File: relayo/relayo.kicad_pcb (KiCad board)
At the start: 2 copper layers, 34 parts, among them J1 24V, J2 Conn_01x02, J3 Conn_01x02, J4 Conn_01x02, J5 DB9_Female, Q1 TIP122, Q2 TIP122, Q3 TIP122, Q4 TIP122, U1 Buck

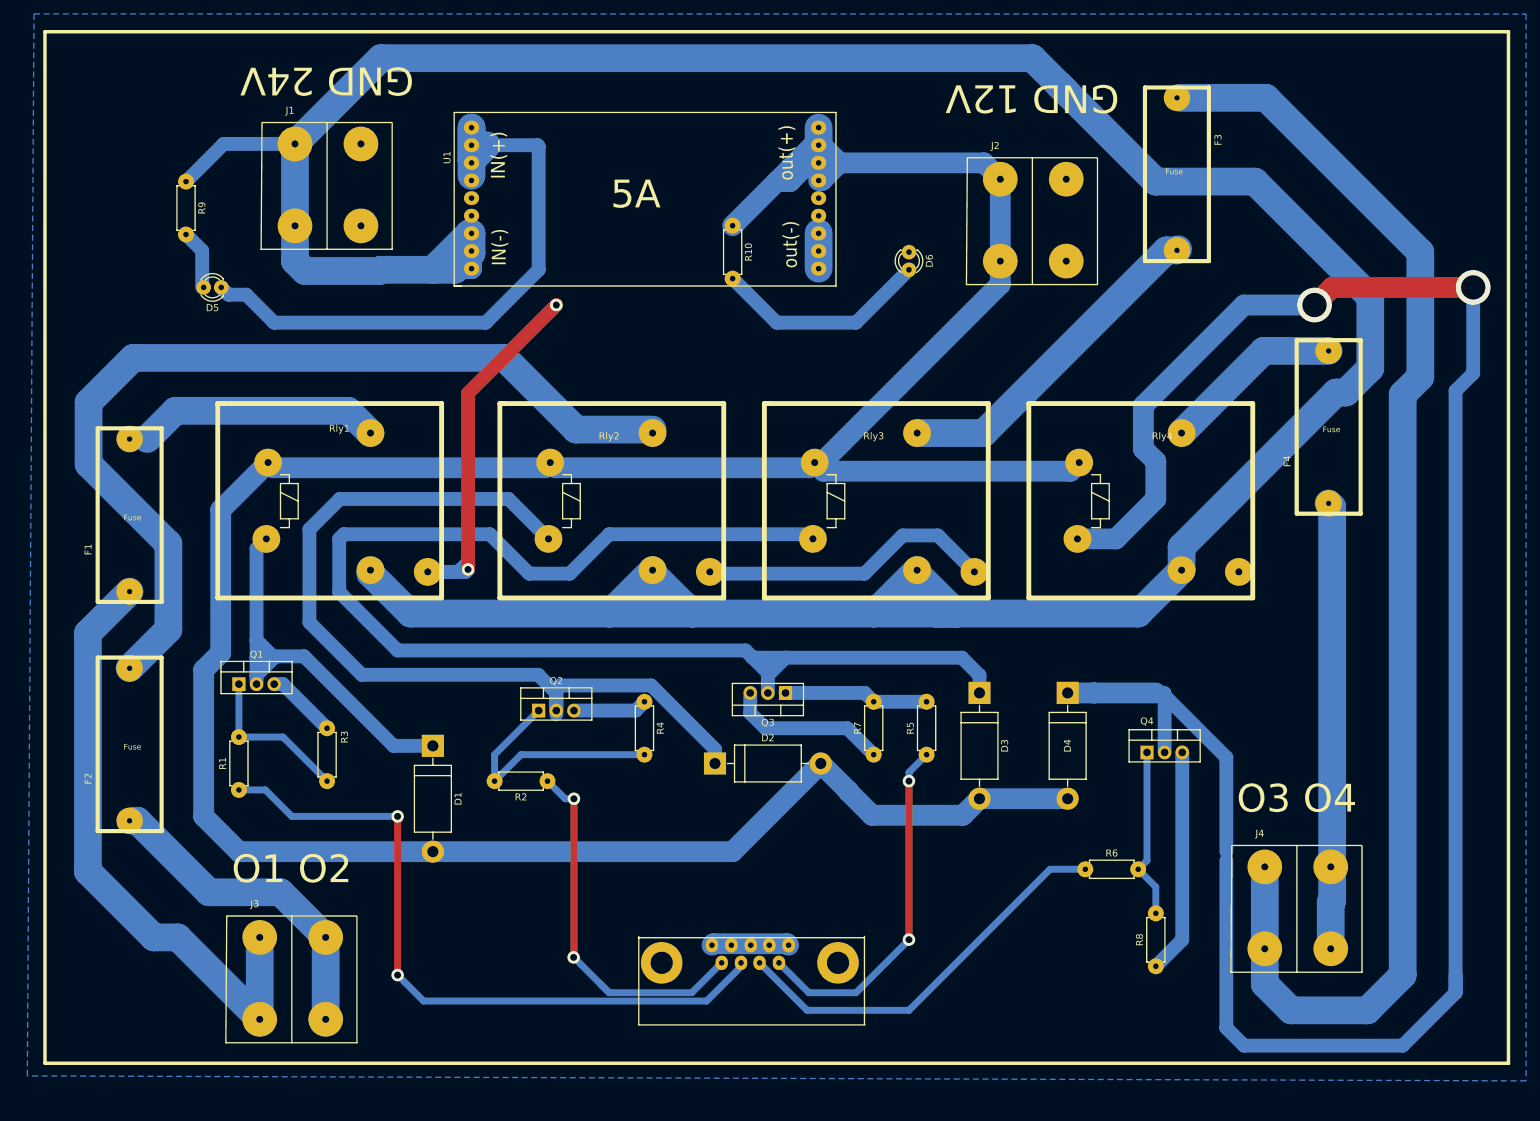
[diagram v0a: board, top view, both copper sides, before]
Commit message: Ckt Desgin done for 4 relay H bridge
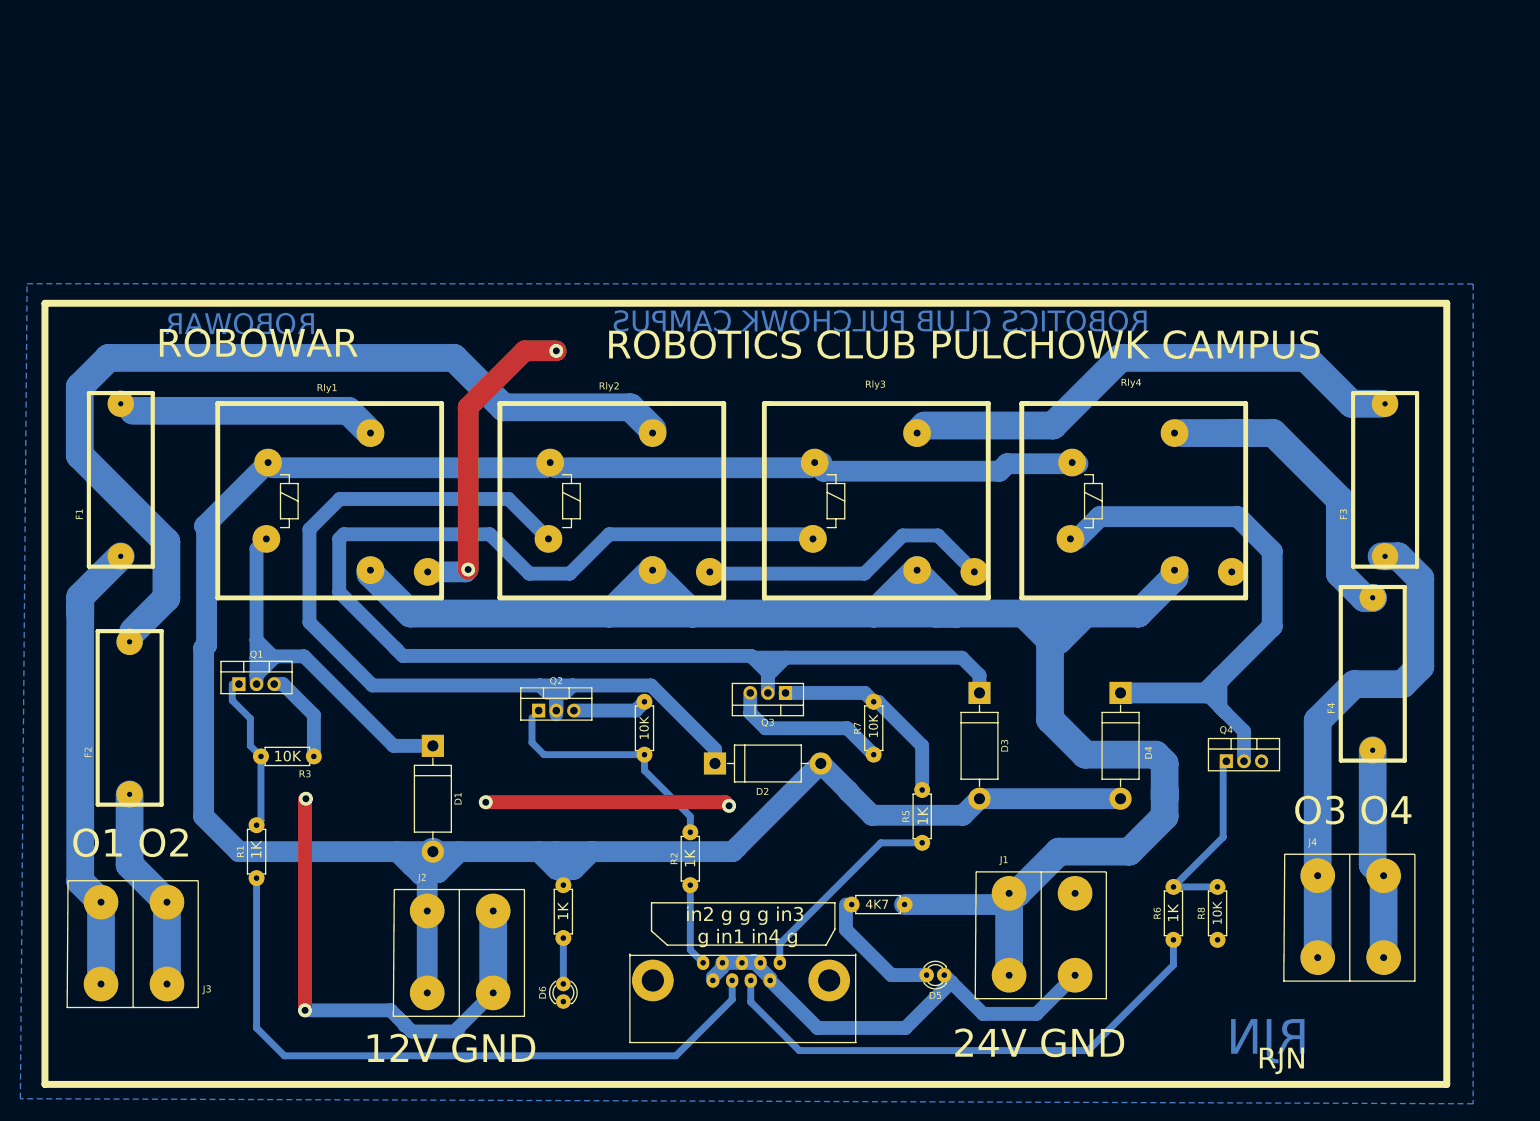
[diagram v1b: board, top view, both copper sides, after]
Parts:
- removed U1: Buck, modFiles:Buck 5A
- moved J1 149.1 mm to (166.4, 143.5)
- moved R9 146.8 mm to (146.7, 139.7), turned to 180 degrees
- moved D5 143.7 mm to (152.4, 149.9)
- moved J2 133.9 mm to (82.5, 146.1)
- moved D6 118.9 mm to (97.5, 153.7), turned to 90 degrees
- moved R10 98.1 mm to (97.5, 136.9)
- moved F3 54.2 mm to (216.4, 78.7), turned to 90 degrees
- moved F4 36.1 mm to (214.6, 106.7)
- moved R2 25.5 mm to (115.8, 136.9), turned to 90 degrees
- moved J3 23.4 mm to (35.6, 144.8)
- moved R6 16.3 mm to (185.4, 144.8), turned to 90 degrees
- moved R1 13.0 mm to (53.3, 135.9)
- moved R5 12.7 mm to (149.2, 130.8)
- moved Q4 11.5 mm to (193.0, 119.1)
- moved R8 9.67 mm to (191.8, 144.8)
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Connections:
- J5 pad 1: GND -> /in3
- J5 pad 5: GND -> /in2
- J5 pad 6: /in3 -> GND
- J5 pad 9: /in2 -> GND
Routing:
- net Net-(D4-Pad1): track 297.8 -> 85.4 mm, vias 2 -> 0
- net /24V: track 481.3 -> 278.9 mm
- net /out3: track 189.5 -> 71.8 mm
- net /12V: track 428.8 -> 370.7 mm
- net /in2: track 54.1 -> 12.4 mm, vias 2 -> 0
- net /out4: track 64.5 -> 30.5 mm
- net GND: track 285.7 -> 312.5 mm, vias 2 -> 6
- net Net-(F3-Pad1): track 48.6 -> 74.1 mm
- net Net-(D6-Pad2): track 31.2 -> 6.10 mm
- net /in3: track 51.4 -> 29.3 mm, vias 2 -> 0
- net /out1: track 88.2 -> 66.5 mm
- net Net-(F4-Pad1): track 26.1 -> 46.2 mm
- net /in4: track 58.2 -> 75.6 mm
- net /out2: track 46.5 -> 29.6 mm
- net Net-(D5-Pad2): track 8.59 -> 17.9 mm
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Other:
- board text added: "12V GND"
- board text added: "24V GND"
- board text added: "RJN"
- board text added: "ROBOTICS CLUB PULCHOWK CAMPUS"
- board text added: "ROBOWAR"
- board text added: "in2 g g g in3 g in1 in4 g"
- board text removed: "5A"
- board text removed: "GND 12V"
- board text removed: "GND 24V"

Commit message: Now Done
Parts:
- added H1: MountingHole, MountingHole:MountingHole_4mm, F.Cu at (218.2, 158.9)
- added H2: MountingHole, MountingHole:MountingHole_4mm, F.Cu at (26.5, 56.6)
- added H3: MountingHole, MountingHole:MountingHole_4mm, F.Cu at (26.8, 159.4)
- added H4: MountingHole, MountingHole:MountingHole_4mm, F.Cu at (218.4, 59.1)
- moved J4 4.13 mm to (206.8, 141.7)
- moved J3 3.43 mm to (39.0, 144.7)
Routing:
- net /out3: track 71.8 -> 74.2 mm
- net GND: track 312.5 -> 310.8 mm
- net /out2: track 29.6 -> 30.9 mm
- net /out1: track 66.5 -> 67.8 mm
- net /out4: track 30.5 -> 31.7 mm

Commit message: residue
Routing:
- net /12V: track 370.7 -> 331.6 mm
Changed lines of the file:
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@@
   (segment (start 171.59 87.03) (end 174.8 83.82) (width 3) (layer "B.Cu") (net 4))
   (segment (start 174.8 83.82) (end 194.658175 83.82) (width 3) (layer "B.Cu") (net 4))
-  (segment (start 88.3412 63.5508) (end 83.82 68.072) (width 3) (layer "F.Cu") (net 5))
+  (segment (start 88.3412 63.5508) (end 83.82 68.072) (width 1) (layer "F.Cu") (net 5))
+  (segment (start 83.82 68.072) (end 83.82 91.44) (width 1) (layer "F.Cu") (net 5))
   (segment (start 120.904 124.968) (end 121.412 125.476) (width 2) (layer "F.Cu") (net 5))
   (segment (start 60.325 124.587) (end 60.452 124.46) (width 2) (layer "F.Cu") (net 5))
-  (segment (start 60.325 154.94) (end 60.325 124.587) (width 2) (layer "F.Cu") (net 5))
-  (segment (start 86.36 124.968) (end 120.904 124.968) (width 2) (layer "F.Cu") (net 5))
-  (segment (start 83.82 68.072) (end 83.82 91.44) (width 3) (layer "F.Cu") (net 5))
-  (segment (start 88.3412 55.6768) (end 88.3412 63.5508) (width 3) (layer "F.Cu") (net 5))
+  (segment (start 60.325 154.94) (end 60.325 124.587) (width 1) (layer "F.Cu") (net 5))
+  (segment (start 86.36 124.968) (end 120.904 124.968) (width 1) (layer "F.Cu") (net 5))
+  (segment (start 88.3412 55.6768) (end 88.3412 63.5508) (width 1) (layer "F.Cu") (net 5))
   (segment (start 88.2904 55.626) (end 88.3412 55.6768) (width 3) (layer "F.Cu") (net 5))
   (via (at 83.82 91.44) (size 2) (drill 1) (layers "F.Cu" "B.Cu") (net 5))
@@
   (segment (start 73.66 132.08) (end 82.55 132.08) (width 3) (layer "B.Cu") (net 17))
   (segment (start 93.98 132.08) (end 96.52 132.08) (width 3) (layer "B.Cu") (net 17))
-  (segment (start 94.89 76.78) (end 55.75 76.78) (width 3) (layer "B.Cu") (net 17))
   (segment (start 77.9274 135.4326) (end 77.0126 135.4326) (width 3) (layer "B.Cu") (net 17))
   (segment (start 101.6 132.08) (end 121.92 132.08) (width 3) (layer "B.Cu") (net 17))
